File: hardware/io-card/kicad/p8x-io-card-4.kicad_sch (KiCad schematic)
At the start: 6 parts, among them J1 MABC96R, J3 1x3

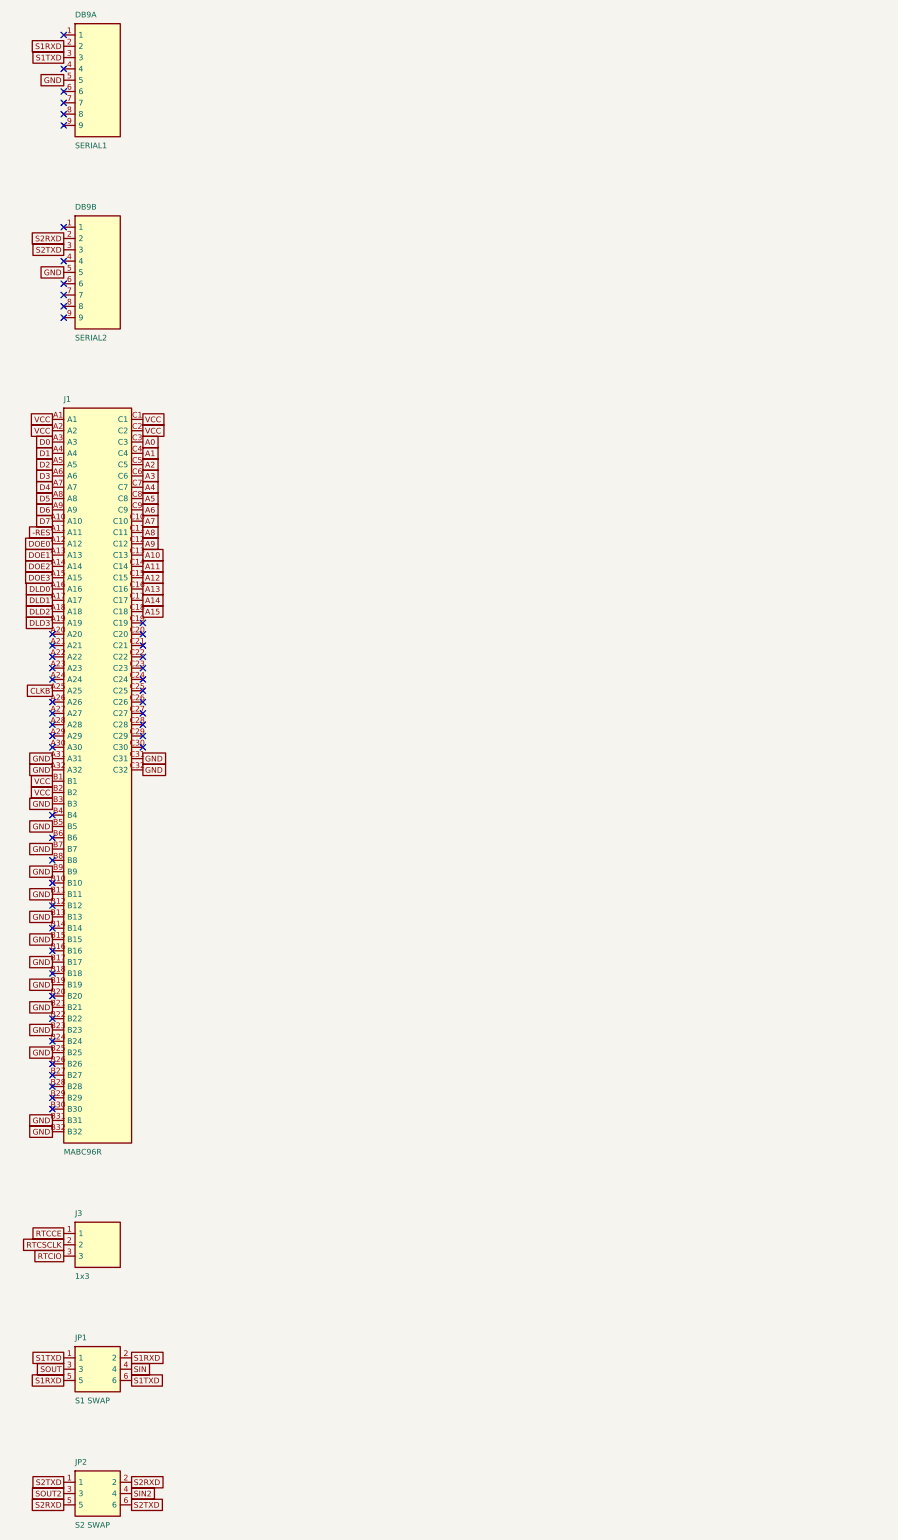
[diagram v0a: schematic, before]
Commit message: feat(sch): draw the io-card schematic by function
Group the io-card into functional sheets (address decode, switch/LED
ports, serial, bus monitor, RTC) with each block's resistors, LEDs,
crystals and connectors on the same sheet, so local nets are drawn as
wires: 18 -> ~330 wires. Orient wires by drawing side on this card
(FLOW_BY_SIDE) so the ACIA -> MAX232 round trip lays out left to right;
put the 6850 and MAX232 bus/TTL pins left and serial/RS-232 pins right;
draw the RX/TX swap jumpers with a schematic-only JMP2X3SWAP variant.
Netlist still matches the board (155 nets, 562 pins), ERC 0 errors.

Co-Authored-By: Claude Opus 5.5 <noreply@anthropic.com>
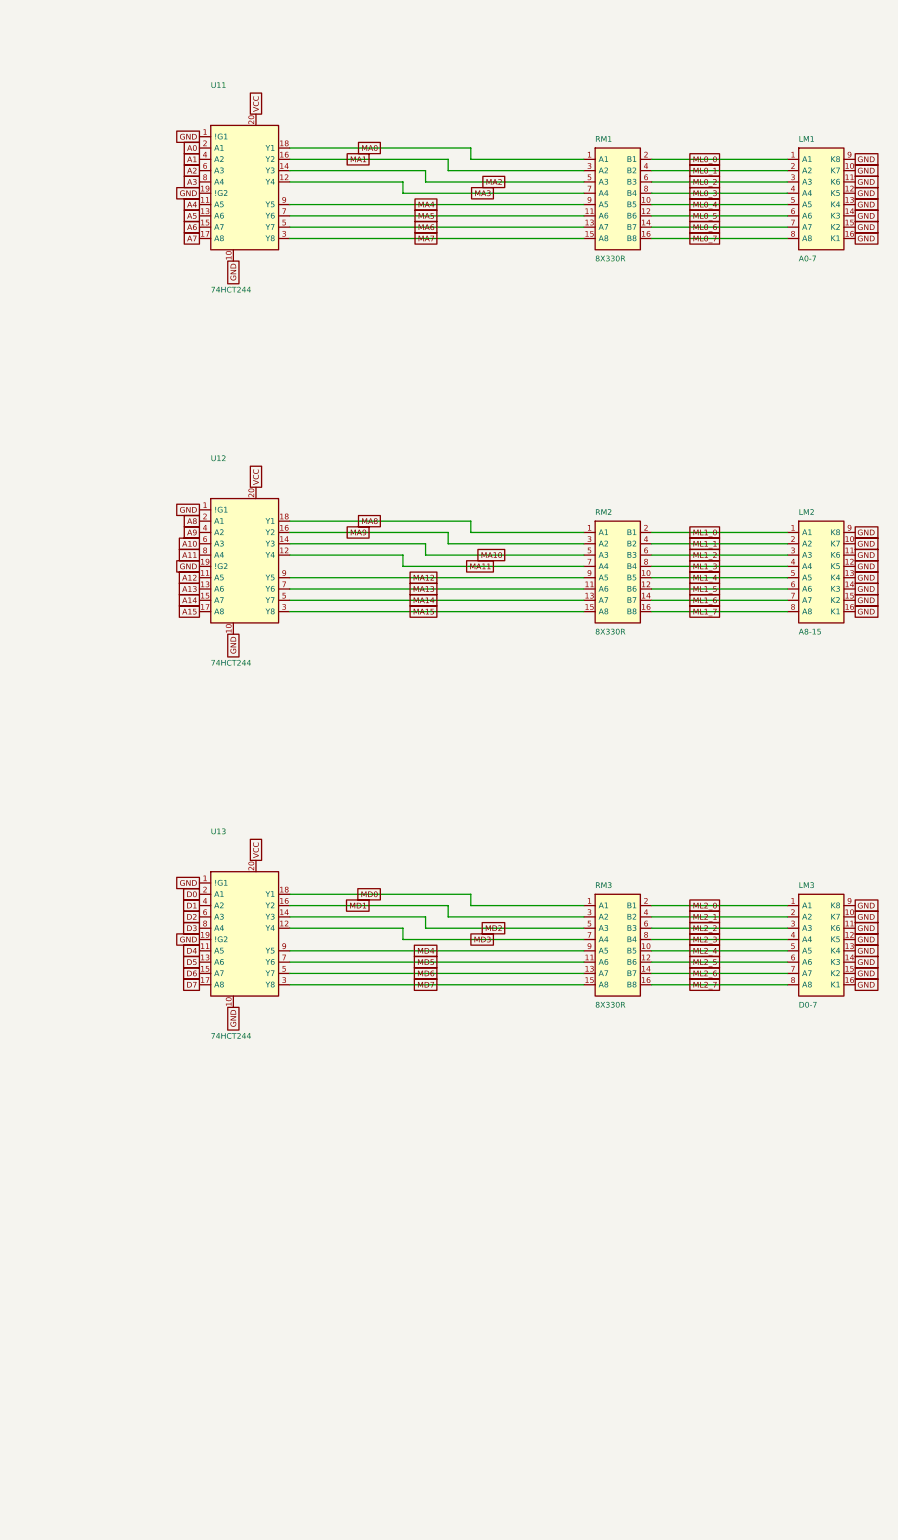
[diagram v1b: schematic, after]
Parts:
- removed DB9A: SERIAL1, Connector_Dsub:DSUB-9_Socket_Horizontal_P2.77x2.54mm_EdgePinOffset9.40mm, symbol p8x:DSUB9F
- removed DB9B: SERIAL2, Connector_Dsub:DSUB-9_Socket_Horizontal_P2.77x2.54mm_EdgePinOffset9.40mm, symbol p8x:DSUB9F
- removed J1: MABC96R, Connector_DIN:DIN41612_C_3x32_Male_Horizontal_THT, symbol p8x:DIN96C
- removed J3: 1x3, Connector_PinHeader_2.54mm:PinHeader_1x03_P2.54mm_Vertical, symbol p8x:HDR3
- removed JP1: S1 SWAP, Connector_PinHeader_2.54mm:PinHeader_2x03_P2.54mm_Vertical, symbol p8x:JMP2X3
- removed JP2: S2 SWAP, Connector_PinHeader_2.54mm:PinHeader_2x03_P2.54mm_Vertical, symbol p8x:JMP2X3
- added LM1: A0-7, Package_DIP:DIP-16_W7.62mm, symbol p8x:LEDARR8
- added LM2: A8-15, Package_DIP:DIP-16_W7.62mm, symbol p8x:LEDARR8
- added LM3: D0-7, Package_DIP:DIP-16_W7.62mm, symbol p8x:LEDARR8
- added RM1, RM2, RM3: 8X330R, Connector_PinHeader_2.54mm:PinHeader_1x16_P2.54mm_Vertical, symbol p8x:RNISO8
- added U11, U12, U13: 74HCT244, Package_DIP:DIP-20_W7.62mm, symbol p8x:74244
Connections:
- net A0: now also U11.2 (A1)
- net A1: now also U11.4 (A2)
- net A10: now also U12.6 (A3)
- net A11: now also U12.8 (A4)
- net A12: now also U12.11 (A5)
- net A13: now also U12.13 (A6)
- net A14: now also U12.15 (A7)
- net A15: now also U12.17 (A8)
- net A2: now also U11.6 (A3)
- net A3: now also U11.8 (A4)
- net A4: now also U11.11 (A5)
- net A5: now also U11.13 (A6)
- net A6: now also U11.15 (A7)
- net A7: now also U11.17 (A8)
- net A8: now also U12.2 (A1)
- net A9: now also U12.4 (A2)
- net D0: now also U13.2 (A1)
- net D1: now also U13.4 (A2)
- net D2: now also U13.6 (A3)
- net D3: now also U13.8 (A4)
- net D4: now also U13.11 (A5)
- net D5: now also U13.13 (A6)
- net D6: now also U13.15 (A7)
- net D7: now also U13.17 (A8)
- net GND: now also LM1.10 (K7), LM1.11 (K6), LM1.12 (K5), LM1.13 (K4), LM1.14 (K3), LM1.15 (K2), LM1.16 (K1), LM1.9 (K8), LM2.10 (K7), LM2.11 (K6), LM2.12 (K5), LM2.13 (K4), LM2.14 (K3), LM2.15 (K2), LM2.16 (K1), LM2.9 (K8), LM3.10 (K7), LM3.11 (K6), LM3.12 (K5), LM3.13 (K4), LM3.14 (K3), LM3.15 (K2), LM3.16 (K1), LM3.9 (K8), U11.1 (!G1), U11.10, U11.19 (!G2), U12.1 (!G1), U12.10, U12.19 (!G2), U13.1 (!G1), U13.10, U13.19 (!G2)
- net VCC: now also U11.20, U12.20, U13.20
- new net MA0: RM1.1 (A1), U11.18 (Y1)
- new net MA1: RM1.3 (A2), U11.16 (Y2)
- new net MA10: RM2.5 (A3), U12.14 (Y3)
- new net MA11: RM2.7 (A4), U12.12 (Y4)
- new net MA12: RM2.9 (A5), U12.9 (Y5)
- new net MA13: RM2.11 (A6), U12.7 (Y6)
- new net MA14: RM2.13 (A7), U12.5 (Y7)
- new net MA15: RM2.15 (A8), U12.3 (Y8)
- new net MA2: RM1.5 (A3), U11.14 (Y3)
- new net MA3: RM1.7 (A4), U11.12 (Y4)
- new net MA4: RM1.9 (A5), U11.9 (Y5)
- new net MA5: RM1.11 (A6), U11.7 (Y6)
- new net MA6: RM1.13 (A7), U11.5 (Y7)
- new net MA7: RM1.15 (A8), U11.3 (Y8)
- new net MA8: RM2.1 (A1), U12.18 (Y1)
- new net MA9: RM2.3 (A2), U12.16 (Y2)
- new net MD0: RM3.1 (A1), U13.18 (Y1)
- new net MD1: RM3.3 (A2), U13.16 (Y2)
- new net MD2: RM3.5 (A3), U13.14 (Y3)
- new net MD3: RM3.7 (A4), U13.12 (Y4)
- new net MD4: RM3.9 (A5), U13.9 (Y5)
- new net MD5: RM3.11 (A6), U13.7 (Y6)
- new net MD6: RM3.13 (A7), U13.5 (Y7)
- new net MD7: RM3.15 (A8), U13.3 (Y8)
- new net ML0_0: LM1.1 (A1), RM1.2 (B1)
- new net ML0_1: LM1.2 (A2), RM1.4 (B2)
- new net ML0_2: LM1.3 (A3), RM1.6 (B3)
- new net ML0_3: LM1.4 (A4), RM1.8 (B4)
- new net ML0_4: LM1.5 (A5), RM1.10 (B5)
- new net ML0_5: LM1.6 (A6), RM1.12 (B6)
- new net ML0_6: LM1.7 (A7), RM1.14 (B7)
- new net ML0_7: LM1.8 (A8), RM1.16 (B8)
- new net ML1_0: LM2.1 (A1), RM2.2 (B1)
- new net ML1_1: LM2.2 (A2), RM2.4 (B2)
- new net ML1_2: LM2.3 (A3), RM2.6 (B3)
- new net ML1_3: LM2.4 (A4), RM2.8 (B4)
- new net ML1_4: LM2.5 (A5), RM2.10 (B5)
- new net ML1_5: LM2.6 (A6), RM2.12 (B6)
- new net ML1_6: LM2.7 (A7), RM2.14 (B7)
- new net ML1_7: LM2.8 (A8), RM2.16 (B8)
- new net ML2_0: LM3.1 (A1), RM3.2 (B1)
- new net ML2_1: LM3.2 (A2), RM3.4 (B2)
- new net ML2_2: LM3.3 (A3), RM3.6 (B3)
- new net ML2_3: LM3.4 (A4), RM3.8 (B4)
- new net ML2_4: LM3.5 (A5), RM3.10 (B5)
- new net ML2_5: LM3.6 (A6), RM3.12 (B6)
- new net ML2_6: LM3.7 (A7), RM3.14 (B7)
- new net ML2_7: LM3.8 (A8), RM3.16 (B8)
- no-connect marks 50 -> 0

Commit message: fix(io): isolated LED resistor banks as DIP-16 networks
RL1 and RM1-RM3 were RNISO8 on a 1x16 pin-header footprint; no
16-pin isolated SIP exists, and the render showed a header. Switch to
RNISO8D (DIP-16), per the WONT-DO resistor packaging rule and matching
the bus test card. Place each network beside its bargraph so pins
16-9 face the anodes straight across; draw them with the straight
RNISO8DSTR schematic variant; BOM names the DIP-16 part and is
regenerated (it was months stale). io-card re-routed: PASS.

Co-Authored-By: Claude Opus 5.5 <noreply@anthropic.com>
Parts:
- RM1, RM2, RM3: footprint Connector_PinHeader_2.54mm:PinHeader_1x16_P2.54mm_Vertical -> Package_DIP:DIP-16_W7.62mm; symbol p8x:RNISO8 -> p8x:RNISO8DSTR
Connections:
- net MA1: now also RM1.2 (A2); no longer RM1.3 (A2)
- net MA10: now also RM2.3 (A3); no longer RM2.5 (A3)
- net MA11: now also RM2.4 (A4); no longer RM2.7 (A4)
- net MA12: now also RM2.5 (A5); no longer RM2.9 (A5)
- net MA13: now also RM2.6 (A6); no longer RM2.11 (A6)
- net MA14: now also RM2.7 (A7); no longer RM2.13 (A7)
- net MA15: now also RM2.8 (A8); no longer RM2.15 (A8)
- net MA2: now also RM1.3 (A3); no longer RM1.5 (A3)
- net MA3: now also RM1.4 (A4); no longer RM1.7 (A4)
- net MA4: now also RM1.5 (A5); no longer RM1.9 (A5)
- net MA5: now also RM1.6 (A6); no longer RM1.11 (A6)
- net MA6: now also RM1.7 (A7); no longer RM1.13 (A7)
- net MA7: now also RM1.8 (A8); no longer RM1.15 (A8)
- net MA9: now also RM2.2 (A2); no longer RM2.3 (A2)
- net MD1: now also RM3.2 (A2); no longer RM3.3 (A2)
- net MD2: now also RM3.3 (A3); no longer RM3.5 (A3)
- net MD3: now also RM3.4 (A4); no longer RM3.7 (A4)
- net MD4: now also RM3.5 (A5); no longer RM3.9 (A5)
- net MD5: now also RM3.6 (A6); no longer RM3.11 (A6)
- net MD6: now also RM3.7 (A7); no longer RM3.13 (A7)
- net MD7: now also RM3.8 (A8); no longer RM3.15 (A8)
- net ML0_0: now also RM1.16 (B1); no longer RM1.2 (B1)
- net ML0_1: now also RM1.15 (B2); no longer RM1.4 (B2)
- net ML0_2: now also RM1.14 (B3); no longer RM1.6 (B3)
- net ML0_3: now also RM1.13 (B4); no longer RM1.8 (B4)
- net ML0_4: now also RM1.12 (B5); no longer RM1.10 (B5)
- net ML0_5: now also RM1.11 (B6); no longer RM1.12 (B6)
- net ML0_6: now also RM1.10 (B7); no longer RM1.14 (B7)
- net ML0_7: now also RM1.9 (B8); no longer RM1.16 (B8)
- net ML1_0: now also RM2.16 (B1); no longer RM2.2 (B1)
- net ML1_1: now also RM2.15 (B2); no longer RM2.4 (B2)
- net ML1_2: now also RM2.14 (B3); no longer RM2.6 (B3)
- net ML1_3: now also RM2.13 (B4); no longer RM2.8 (B4)
- net ML1_4: now also RM2.12 (B5); no longer RM2.10 (B5)
- net ML1_5: now also RM2.11 (B6); no longer RM2.12 (B6)
- net ML1_6: now also RM2.10 (B7); no longer RM2.14 (B7)
- net ML1_7: now also RM2.9 (B8); no longer RM2.16 (B8)
- net ML2_0: now also RM3.16 (B1); no longer RM3.2 (B1)
- net ML2_1: now also RM3.15 (B2); no longer RM3.4 (B2)
- net ML2_2: now also RM3.14 (B3); no longer RM3.6 (B3)
- net ML2_3: now also RM3.13 (B4); no longer RM3.8 (B4)
- net ML2_4: now also RM3.12 (B5); no longer RM3.10 (B5)
- net ML2_5: now also RM3.11 (B6); no longer RM3.12 (B6)
- net ML2_6: now also RM3.10 (B7); no longer RM3.14 (B7)
- net ML2_7: now also RM3.9 (B8); no longer RM3.16 (B8)
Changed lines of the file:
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@@
   (global_label "VCC" (shape passive) (at 68.58 218.44 90) (fields_autoplaced yes) (effects (font (size 1.27 1.27)) (justify left))
     (property "Intersheetrefs" "${INTERSHEET_REFS}" (at 68.58 218.44 0) (effects (font (size 1.27 1.27)) hide)))
-  (symbol (lib_id "p8x:RNISO8") (at 149.86 71.12 0) (unit 1) (in_bom yes) (on_board yes) (dnp no)
+  (symbol (lib_id "p8x:RNISO8DSTR") (at 149.86 71.12 0) (unit 1) (in_bom yes) (on_board yes) (dnp no)
     (property "Reference" "RM1" (at 144.78 56.42 0) (effects (font (size 1.27 1.27)) (justify left)))
     (property "Value" "8X330R" (at 144.78 83.28 0) (effects (font (size 1.27 1.27)) (justify left)))
-    (property "Footprint" "Connector_PinHeader_2.54mm:PinHeader_1x16_P2.54mm_Vertical" (at 149.86 71.12 0) (effects (font (size 1.27 1.27)) hide))
+    (property "Footprint" "Package_DIP:DIP-16_W7.62mm" (at 149.86 71.12 0) (effects (font (size 1.27 1.27)) hide))
     (property "Datasheet" "" (at 149.86 71.12 0) (effects (font (size 1.27 1.27)) hide))
     (pin "1")
+    (pin "2")
     (pin "3")
+    (pin "4")
     (pin "5")
+    (pin "6")
     (pin "7")
+    (pin "8")
+    (pin "16")
+    (pin "15")
+    (pin "14")
+    (pin "13")
+    (pin "12")
+    (pin "11")
+    (pin "10")
     (pin "9")
-    (pin "11")
-    (pin "13")
-    (pin "15")
-    (pin "2")
-    (pin "4")
-    (pin "6")
-    (pin "8")
-    (pin "10")
-    (pin "12")
-    (pin "14")
-    (pin "16")
     (instances (project "p8x-io-card" (path "/ed807a3d-9122-5982-9811-120926e12b80/c02bb545-6ccf-5d1f-b951-d87b26d77293" (reference "RM1") (unit 1))))
   )
-  (symbol (lib_id "p8x:RNISO8") (at 149.86 154.94 0) (unit 1) (in_bom yes) (on_board yes) (dnp no)
+  (symbol (lib_id "p8x:RNISO8DSTR") (at 149.86 154.94 0) (unit 1) (in_bom yes) (on_board yes) (dnp no)
     (property "Reference" "RM2" (at 144.78 140.24 0) (effects (font (size 1.27 1.27)) (justify left)))
     (property "Value" "8X330R" (at 144.78 167.10 0) (effects (font (size 1.27 1.27)) (justify left)))
-    (property "Footprint" "Connector_PinHeader_2.54mm:PinHeader_1x16_P2.54mm_Vertical" (at 149.86 154.94 0) (effects (font (size 1.27 1.27)) hide))
+    (property "Footprint" "Package_DIP:DIP-16_W7.62mm" (at 149.86 154.94 0) (effects (font (size 1.27 1.27)) hide))
     (property "Datasheet" "" (at 149.86 154.94 0) (effects (font (size 1.27 1.27)) hide))
     (pin "1")
+    (pin "2")
     (pin "3")
+    (pin "4")
     (pin "5")
+    (pin "6")
     (pin "7")
+    (pin "8")
+    (pin "16")
+    (pin "15")
+    (pin "14")
+    (pin "13")
+    (pin "12")
+    (pin "11")
+    (pin "10")
     (pin "9")
-    (pin "11")
-    (pin "13")
-    (pin "15")
-    (pin "2")
-    (pin "4")
-    (pin "6")
-    (pin "8")
-    (pin "10")
-    (pin "12")
-    (pin "14")
-    (pin "16")
     (instances (project "p8x-io-card" (path "/ed807a3d-9122-5982-9811-120926e12b80/c02bb545-6ccf-5d1f-b951-d87b26d77293" (reference "RM2") (unit 1))))
   )
-  (symbol (lib_id "p8x:RNISO8") (at 149.86 238.76 0) (unit 1) (in_bom yes) (on_board yes) (dnp no)
+  (symbol (lib_id "p8x:RNISO8DSTR") (at 149.86 238.76 0) (unit 1) (in_bom yes) (on_board yes) (dnp no)
     (property "Reference" "RM3" (at 144.78 224.06 0) (effects (font (size 1.27 1.27)) (justify left)))
     (property "Value" "8X330R" (at 144.78 250.92 0) (effects (font (size 1.27 1.27)) (justify left)))
-    (property "Footprint" "Connector_PinHeader_2.54mm:PinHeader_1x16_P2.54mm_Vertical" (at 149.86 238.76 0) (effects (font (size 1.27 1.27)) hide))
+    (property "Footprint" "Package_DIP:DIP-16_W7.62mm" (at 149.86 238.76 0) (effects (font (size 1.27 1.27)) hide))
     (property "Datasheet" "" (at 149.86 238.76 0) (effects (font (size 1.27 1.27)) hide))
     (pin "1")
+    (pin "2")
     (pin "3")
+    (pin "4")
     (pin "5")
+    (pin "6")
     (pin "7")
+    (pin "8")
+    (pin "16")
+    (pin "15")
+    (pin "14")
+    (pin "13")
+    (pin "12")
+    (pin "11")
+    (pin "10")
     (pin "9")
-    (pin "11")
-    (pin "13")
-    (pin "15")
-    (pin "2")
-    (pin "4")
-    (pin "6")
-    (pin "8")
-    (pin "10")
-    (pin "12")
-    (pin "14")
-    (pin "16")
     (instances (project "p8x-io-card" (path "/ed807a3d-9122-5982-9811-120926e12b80/c02bb545-6ccf-5d1f-b951-d87b26d77293" (reference "RM3") (unit 1))))
   )
